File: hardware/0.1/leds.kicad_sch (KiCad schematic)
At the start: 22 parts

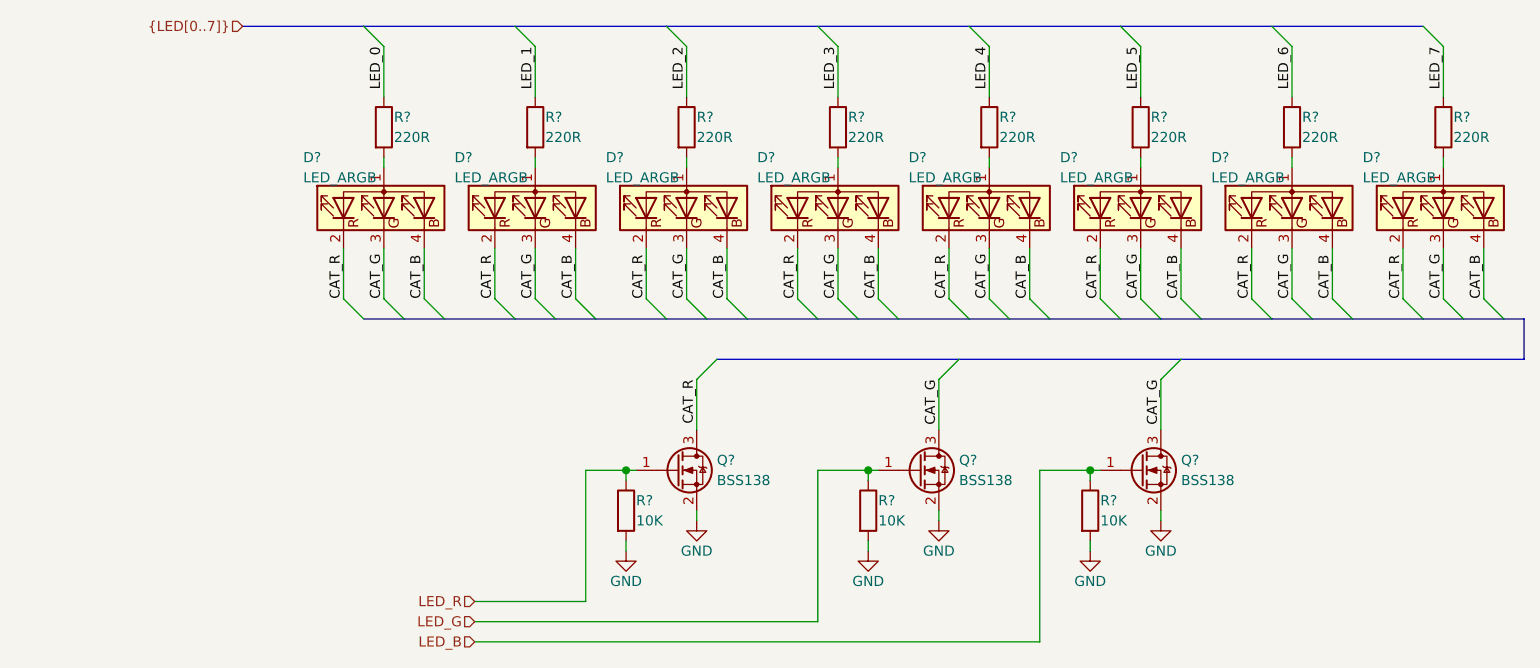
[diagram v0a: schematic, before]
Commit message: all 3d models added
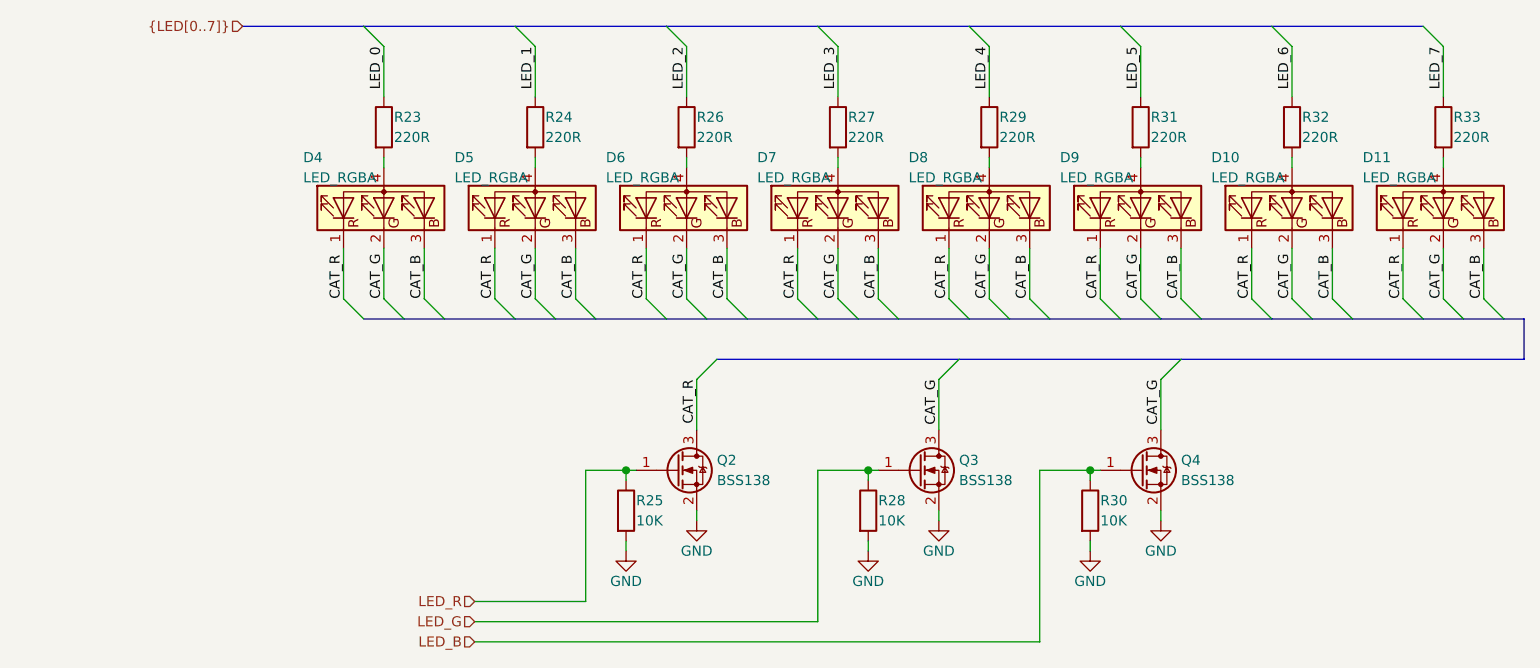
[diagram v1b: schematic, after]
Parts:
- removed D? (x8): LED_ARGB, symbol Device:LED_ARGB
- added D10, D11, D4, D5, D6, D7, D8, D9: LED_RGBA, josh-led:LED_0606_E6C0606RGBC3UDA, symbol josh-led:LED_RGBA
- Q2, Q3, Q4: renamed from Q?; footprint Package_TO_SOT_SMD:SOT-23 -> Package_TO_SOT_SMD:SOT-323_SC-70
- R23, R24, R25, R26, R27, R28, R29, R30, R31, R32, R33: renamed from R?; footprint (none) -> Resistor_SMD:R_0402_1005Metric
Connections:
- net CAT_B: now also D10.3 (BK), D11.3 (BK), D4.3 (BK), D5.3 (BK), D6.3 (BK), D7.3 (BK), D8.3 (BK), D9.3 (BK)
- net CAT_G: now also D10.2 (GK), D11.2 (GK), D4.2 (GK), D5.2 (GK), D6.2 (GK), D7.2 (GK), D8.2 (GK), D9.2 (GK)
- net CAT_R: now also D10.1 (RK), D11.1 (RK), D4.1 (RK), D5.1 (RK), D6.1 (RK), D7.1 (RK), D8.1 (RK), D9.1 (RK)
- net at R26.2: now also D6.4 (A)
- net at R24.2: now also D5.4 (A)
- net at R27.2: now also D7.4 (A)
- net at R31.2: now also D9.4 (A)
- net at R23.2: now also D4.4 (A)
- net at R32.2: now also D10.4 (A)
- net at R29.2: now also D8.4 (A)
- net at R33.2: now also D11.4 (A)

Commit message: layout ++
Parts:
- removed R23, R24, R26, R27, R29, R31, R32, R33: 220R, Resistor_SMD:R_0402_1005Metric, symbol Device:R
- added RN2, RN3: 220R, Resistor_SMD:R_Array_Convex_4x0402, symbol josh-passive:RN
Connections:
- net LED_0: now also RN2.5
- net LED_1: now also RN2.6
- net LED_2: now also RN2.7
- net LED_3: now also RN2.8
- net LED_4: now also RN3.5
- net LED_5: now also RN3.6
- net LED_6: now also RN3.7
- net LED_7: now also RN3.8
- net at D5.4 (A): now also RN2.3
- net at D10.4 (A): now also RN3.2
- net at D8.4 (A): now also RN3.4
- net at D4.4 (A): now also RN2.4
- net at D9.4 (A): now also RN3.3
- net at D7.4 (A): now also RN2.1
- net at D6.4 (A): now also RN2.2
- net at D11.4 (A): now also RN3.1

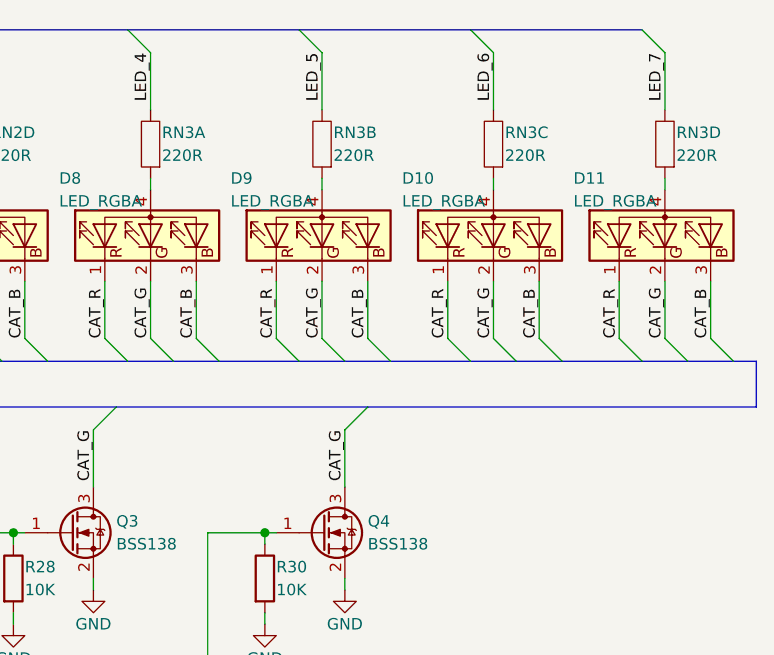
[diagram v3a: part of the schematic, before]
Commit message: half IO laid out
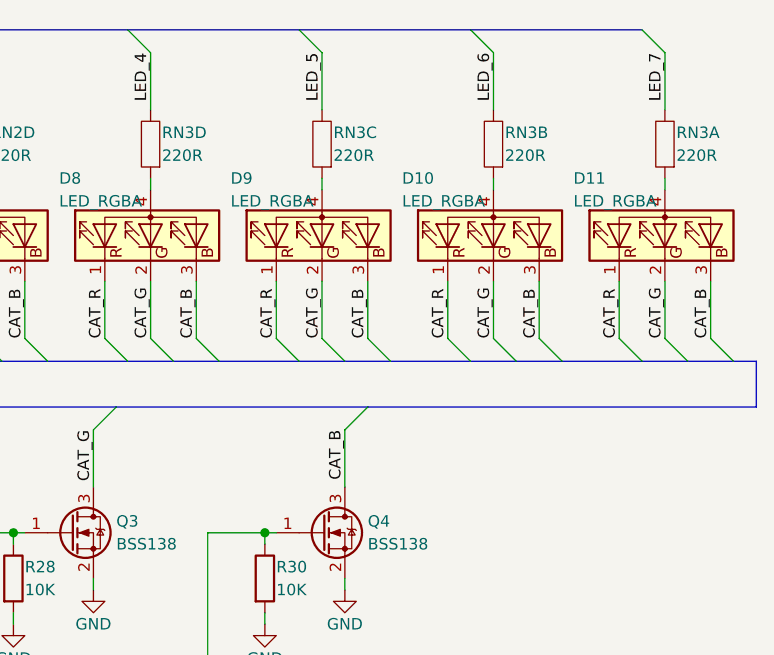
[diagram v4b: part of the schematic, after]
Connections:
- net CAT_B: now also Q4.3 (D)
- net CAT_G: no longer Q4.3 (D)
- net LED_4: now also RN3.8; no longer RN3.5
- net LED_5: now also RN3.7; no longer RN3.6
- net LED_6: now also RN3.6; no longer RN3.7
- net LED_7: now also RN3.5; no longer RN3.8
- net at D10.4 (A): now also RN3.3; no longer RN3.2
- net at D8.4 (A): now also RN3.1; no longer RN3.4
- net at D11.4 (A): now also RN3.4; no longer RN3.1
- net at D9.4 (A): now also RN3.2; no longer RN3.3
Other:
- moved on the sheet: RN3A, RN3B, RN3C, RN3D
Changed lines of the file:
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@@
     (effects (font (size 1.27 1.27)) (justify left bottom))
   )
-  (label "CAT_G" (at 190.5 114.3 270)
+  (label "CAT_B" (at 190.5 114.3 270)
     (effects (font (size 1.27 1.27)) (justify right bottom))
   )
@@
     )
   )
-  (symbol (lib_id "josh-passive:RN") (at 168.91 82.55 90) (unit 1)
+  (symbol (lib_id "josh-passive:RN") (at 168.91 82.55 90) (unit 4)
     (in_bom yes) (on_board yes)
     (property "Reference" "RN3" (id 0) (at 170.18 81.28 90)
@@
     )
   )
-  (symbol (lib_id "josh-passive:RN") (at 187.96 82.55 90) (unit 2)
+  (symbol (lib_id "josh-passive:RN") (at 187.96 82.55 90) (unit 3)
     (in_bom yes) (on_board yes)
     (property "Reference" "RN3" (id 0) (at 189.23 81.28 90)
@@
     )
   )
-  (symbol (lib_id "josh-passive:RN") (at 207.01 82.55 90) (unit 3)
+  (symbol (lib_id "josh-passive:RN") (at 207.01 82.55 90) (unit 2)
     (in_bom yes) (on_board yes)
     (property "Reference" "RN3" (id 0) (at 208.28 81.28 90)
@@
     )
   )
-  (symbol (lib_id "josh-passive:RN") (at 226.06 82.55 90) (unit 4)
+  (symbol (lib_id "josh-passive:RN") (at 226.06 82.55 90) (unit 1)
     (in_bom yes) (on_board yes)
     (property "Reference" "RN3" (id 0) (at 227.33 81.28 90)

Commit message: half IO routed
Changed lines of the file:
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@@
   (junction (at 153.67 125.73) (diameter 1.016) (color 0 0 0 0))
   (junction (at 181.61 125.73) (diameter 1.016) (color 0 0 0 0))
+  (junction (at 76.2 69.85) (diameter 1.016) (color 0 0 0 0))
   (bus_entry (at 87.63 104.14) (size 2.54 2.54)
     (stroke (width 0.1524) (type solid) (color 0 0 0 0))
@@
     (stroke (width 0.1524) (type solid) (color 0 0 0 0))
   )
+  (bus_entry (at 101.6 139.7) (size 2.54 2.54)
+    (stroke (width 0.1524) (type solid) (color 0 0 0 0))
+  )
+  (bus_entry (at 101.6 142.24) (size 2.54 2.54)
+    (stroke (width 0.1524) (type solid) (color 0 0 0 0))
+  )
+  (bus_entry (at 101.6 144.78) (size 2.54 2.54)
+    (stroke (width 0.1524) (type solid) (color 0 0 0 0))
+  )
   (bus_entry (at 106.68 104.14) (size 2.54 2.54)
     (stroke (width 0.1524) (type solid) (color 0 0 0 0))
@@
     (stroke (width 0) (type solid) (color 0 0 0 0))
   )
-  (bus (pts (xy 74.93 69.85) (xy 90.17 69.85))
+  (bus (pts (xy 54.61 69.85) (xy 76.2 69.85))
+    (stroke (width 0) (type solid) (color 0 0 0 0))
+  )
+  (bus (pts (xy 76.2 69.85) (xy 90.17 69.85))
+    (stroke (width 0) (type solid) (color 0 0 0 0))
+  )
+  (bus (pts (xy 76.2 113.03) (xy 76.2 69.85))
     (stroke (width 0) (type solid) (color 0 0 0 0))
   )
@@
     (stroke (width 0) (type solid) (color 0 0 0 0))
   )
+  (bus (pts (xy 101.6 113.03) (xy 76.2 113.03))
+    (stroke (width 0) (type solid) (color 0 0 0 0))
+  )
+  (bus (pts (xy 101.6 113.03) (xy 101.6 139.7))
+    (stroke (width 0) (type solid) (color 0 0 0 0))
+  )
+  (bus (pts (xy 101.6 139.7) (xy 101.6 142.24))
+    (stroke (width 0) (type solid) (color 0 0 0 0))
+  )
+  (bus (pts (xy 101.6 142.24) (xy 101.6 144.78))
+    (stroke (width 0) (type solid) (color 0 0 0 0))
+  )
   (bus (pts (xy 109.22 69.85) (xy 128.27 69.85))
     (stroke (width 0) (type solid) (color 0 0 0 0))
@@
     (effects (font (size 1.27 1.27)) (justify left bottom))
   )
+  (label "LED_R" (at 107.95 142.24 0)
+    (effects (font (size 1.27 1.27)) (justify left bottom))
+  )
+  (label "LED_G" (at 107.95 144.78 0)
+    (effects (font (size 1.27 1.27)) (justify left bottom))
+  )
+  (label "LED_B" (at 107.95 147.32 0)
+    (effects (font (size 1.27 1.27)) (justify left bottom))
+  )
   (label "LED_1" (at 111.76 72.39 270)
     (effects (font (size 1.27 1.27)) (justify right bottom))
@@
     (effects (font (size 1.27 1.27)) (justify left bottom))
   )
-  (hierarchical_label "{LED}" (shape input) (at 74.93 69.85 180)
+  (hierarchical_label "{LED}" (shape input) (at 54.61 69.85 180)
     (effects (font (size 1.27 1.27)) (justify right))
   )
-  (hierarchical_label "LED_R" (shape input) (at 104.14 142.24 180)
-    (effects (font (size 1.27 1.27)) (justify right))
-  )
-  (hierarchical_label "LED_G" (shape input) (at 104.14 144.78 180)
-    (effects (font (size 1.27 1.27)) (justify right))
-  )
-  (hierarchical_label "LED_B" (shape input) (at 104.14 147.32 180)
-    (effects (font (size 1.27 1.27)) (justify right))
-  )

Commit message: all DRC / ERC errors signed off
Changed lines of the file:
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@@
   (page 2 5)
   (paper "A4")
+  (bus_alias "LED_CAT" (members "CAT_R" "CAT_G" "CAT_B"))
   (junction (at 123.19 125.73) (diameter 1.016) (color 0 0 0 0))
   (junction (at 153.67 125.73) (diameter 1.016) (color 0 0 0 0))
@@
     (effects (font (size 1.27 1.27)) (justify left bottom))
   )
+  (label "{LED_CAT}" (at 175.26 111.76 0)
+    (effects (font (size 1.27 1.27)) (justify left bottom))
+  )
